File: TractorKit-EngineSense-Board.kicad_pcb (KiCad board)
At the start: 2 copper layers, 57.5 x 45 mm, 24 parts, among them J1 POWER, J2 ADC1, J3 ADC2, J4 UART, J5 I2C, U1 AMS1117-3.3, U2 ACS711xLCTR-12AB, U3 ESP32-WROOM-32

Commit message: First complete draft.
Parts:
- removed TP1: SERVICE_BOOT, TestPoint:TestPoint_Pad_D1.5mm
- removed TP2: SERVICE_TX, TestPoint:TestPoint_Pad_D1.5mm
- removed TP3: SERVICE_RX, TestPoint:TestPoint_Pad_D1.5mm
- removed TP5: SERVICE_GND, TestPoint:TestPoint_Pad_D1.5mm
- added  : , open-agri.github.io/TKES1, B.Cu at (59.8, 65.2)
- added  : MountingHole_3.2mm_M3_DIN965_Pad, MountingHole:MountingHole_3.2mm_M3_DIN965_Pad, F.Cu at (81.8, 87.0)
- added  : MountingHole_3.2mm_M3_DIN965_Pad, MountingHole:MountingHole_3.2mm_M3_DIN965_Pad, F.Cu at (124.2, 60.7)
- added  : MountingHole_3.2mm_M3_DIN965_Pad, MountingHole:MountingHole_3.2mm_M3_DIN965_Pad, F.Cu at (75.0, 61.0)
- added BOOT: SERVICE_BOOT, TestPoint:TestPoint_Pad_D1.5mm, F.Cu at (108.6, 87.6)
- added GND: SERVICE_GND, TestPoint:TestPoint_Pad_D1.5mm, F.Cu at (93.3, 87.6)
- added R10: 1k, Resistor_THT:R_Axial_DIN0207_L6.3mm_D2.5mm_P10.16mm_Horizontal, F.Cu at (122.9, 76.2)
- added R11: 1k, Resistor_THT:R_Axial_DIN0207_L6.3mm_D2.5mm_P10.16mm_Horizontal, F.Cu at (119.9, 76.2)
- added R12: 1k, Resistor_THT:R_Axial_DIN0207_L6.3mm_D2.5mm_P10.16mm_Horizontal, F.Cu at (116.8, 76.2)
- added R13: 1k, Resistor_THT:R_Axial_DIN0207_L6.3mm_D2.5mm_P10.16mm_Horizontal, F.Cu at (113.8, 76.2)
- added R4: 10k, Resistor_THT:R_Axial_DIN0207_L6.3mm_D2.5mm_P10.16mm_Horizontal, F.Cu at (126.0, 88.9)
- added R5: 10k, Resistor_THT:R_Axial_DIN0207_L6.3mm_D2.5mm_P10.16mm_Horizontal, F.Cu at (122.9, 88.9)
- added R6: 10k, Resistor_THT:R_Axial_DIN0207_L6.3mm_D2.5mm_P10.16mm_Horizontal, F.Cu at (119.9, 88.9)
- added R7: 10k, Resistor_THT:R_Axial_DIN0207_L6.3mm_D2.5mm_P10.16mm_Horizontal, F.Cu at (116.8, 88.9)
- added R8: 10k, Resistor_THT:R_Axial_DIN0207_L6.3mm_D2.5mm_P10.16mm_Horizontal, F.Cu at (113.8, 88.9)
- added R9: 1k, Resistor_THT:R_Axial_DIN0207_L6.3mm_D2.5mm_P10.16mm_Horizontal, F.Cu at (126.0, 76.2)
- added RX: SERVICE_RX, TestPoint:TestPoint_Pad_D1.5mm, F.Cu at (101.0, 87.6)
- added TX: SERVICE_TX, TestPoint:TestPoint_Pad_D1.5mm, F.Cu at (104.8, 87.6)
- moved R3 33.5 mm to (85.7, 83.8), turned to 90 degrees
- moved U1 27.5 mm to (73.7, 85.1)
- moved R1 24.8 mm to (72.4, 78.1), turned to 90 degrees
- moved 3V3 23.8 mm to (97.2, 87.6), turned to 180 degrees
- moved J3 23.3 mm to (125.0, 95.0), turned to 180 degrees
- moved C6 23.1 mm to (85.6, 66.0), turned to 180 degrees
- moved J2 22.3 mm to (110.0, 95.0), turned to 180 degrees
- moved R2 21.8 mm to (76.2, 67.9), turned to 270 degrees
- moved C1 18.6 mm to (65.4, 74.3), turned to 180 degrees
- moved C5 17.0 mm to (55.3, 64.1)
- moved C7 13.4 mm to (80.7, 69.8)
- moved C2 12.8 mm to (67.3, 87.5), turned to 90 degrees
- moved C4 11.9 mm to (54.6, 77.4), turned to 90 degrees
- moved U3 11.5 mm to (98.5, 72.9)
- moved BYPASS 5.77 mm to (62.7, 86.1)
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- renumbered TP4 to 3V3, JP1 to BYPASS
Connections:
- net Net-(J1-Pad1) renamed /12VIN
- J2 pad 1: Net-(J2-Pad1) -> /ADC1_4
- J2 pad 2: Net-(J2-Pad2) -> /ADC1_7
- J2 pad 3: Net-(J2-Pad3) -> +12V
- J3 pad 1: Net-(J3-Pad1) -> /ADC2_8
- J3 pad 2: Net-(J3-Pad2) -> /ADC2_9
- J3 pad 3: Net-(J3-Pad3) -> /ADC2_7
- J4 pad 1: Net-(J4-Pad1) -> /RX
- J4 pad 2: Net-(J4-Pad2) -> /TX
- U3 pad 27: Net-(U3-Pad27) -> /RX
- U3 pad 28: Net-(U3-Pad28) -> /TX
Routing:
- net +12V: track 0.00 -> 59.6 mm
- net /SCL: track 0.00 -> 51.3 mm
- net +3V3: track 0.00 -> 49.5 mm, vias 0 -> 2
- net /SDA: track 0.00 -> 43.3 mm
- net Net-(R4-Pad2): track 0.00 -> 41.3 mm, vias 0 -> 1
- net /AN_CURR: track 0.00 -> 40.9 mm
- net Net-(R10-Pad1): track 0.00 -> 38.4 mm, vias 0 -> 1
- net Net-(R11-Pad1): track 0.00 -> 35.5 mm, vias 0 -> 1
- net Net-(R12-Pad1): track 0.00 -> 34.1 mm, vias 0 -> 1
- net /PR_RX: track 0.00 -> 32.0 mm
- net Net-(R13-Pad1): track 0.00 -> 30.9 mm, vias 0 -> 1
- net /PR_TX: track 0.00 -> 30.3 mm
- net /TX: track 0.00 -> 27.5 mm
- net /RX: track 0.00 -> 23.3 mm
- net GND: track 0.00 -> 21.7 mm, vias 0 -> 18
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- added copper zone on F.Cu, net +12V
- added copper zone on F.Cu, net +3V3
- added copper zone on F.Cu, net /12VIN
- added copper zone on B.Cu, net GND
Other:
- board size 57.5 x 45 mm -> 76 x 45 mm
- rule pad_to_mask_clearance: 0.051 -> 0
- board text added: "+12V"
- board text added: "+3.3V"
- board text added: "0-36V, NOT PROTECTED ALL INPUTS 11k FOR ADC 2 DISABLE Wi-Fi"
- board text added: "12V POWER INPUT 3.3V OUT 1A MAX"
- board text added: "3.3V"
- board text added: "CH4"
- board text added: "CH7"
- board text added: "CH8"
- board text added: "CH9"
- board text added: "EngineSense 1.0 Riccardo Persello ©2020 OpenAgri Model number TKES1 Board S/N: JLCJLCJLCJLC"
- board text added: "GND"
- board text added: "I2C"
- board text added: "INPUT"
- board text added: "IO25"
- board text added: "IO26"
- board text added: "IO27"
- board text added: "OUT"
- board text added: "POWER"
- board text added: "RX"
- board text added: "SAR ADC 1"
- board text added: "SAR ADC 2 / GPIO"
- board text added: "SCL"
- board text added: "SDA"
- board text added: "SERIAL"
- board text added: "SERIAL/I2C 3.3V ONLY NOT PROTECTED NO 5V TOLERANCE"
- board text added: "TX"

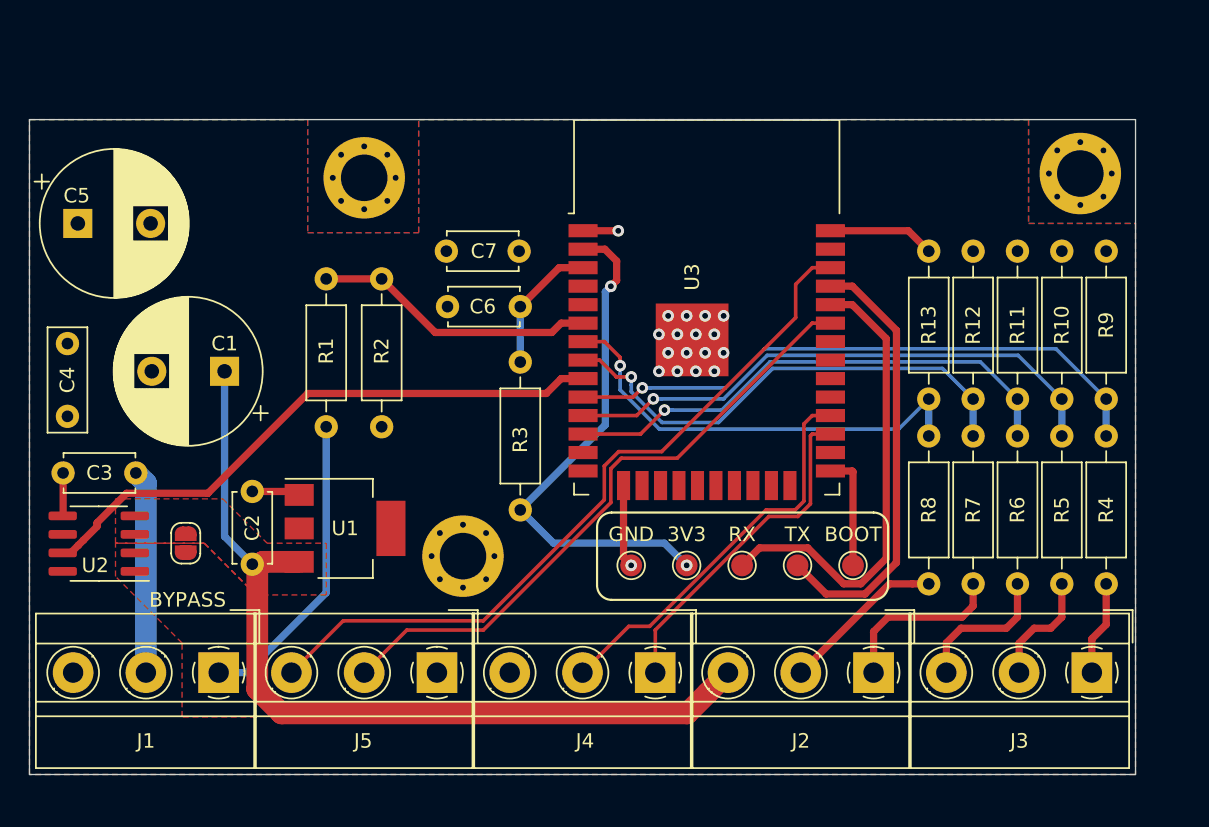
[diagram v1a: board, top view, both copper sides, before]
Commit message: Moved to SMD components
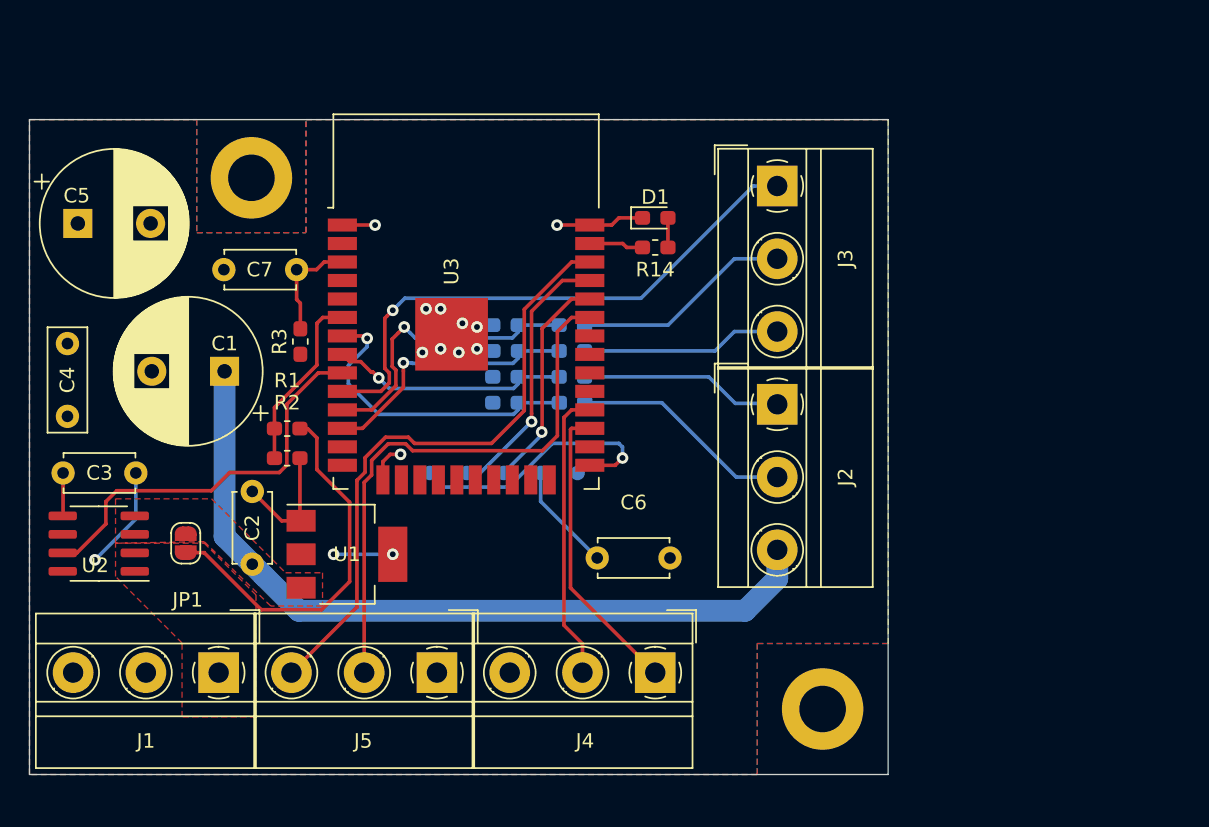
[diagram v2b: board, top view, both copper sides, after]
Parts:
- removed the   at (81.8, 87.0)
- removed the   at (124.2, 60.7)
- removed the   at (75.0, 61.0)
- removed 3V3: SERVICE_3V3, TestPoint:TestPoint_Pad_D1.5mm
- removed BOOT: SERVICE_BOOT, TestPoint:TestPoint_Pad_D1.5mm
- removed GND: SERVICE_GND, TestPoint:TestPoint_Pad_D1.5mm
- removed R4: 10k, Resistor_THT:R_Axial_DIN0207_L6.3mm_D2.5mm_P10.16mm_Horizontal
- removed R9: 1k, Resistor_THT:R_Axial_DIN0207_L6.3mm_D2.5mm_P10.16mm_Horizontal
- removed the RX at (101.0, 87.6)
- removed the TX at (104.8, 87.6)
- added  : MountingHole_3.2mm_M3_DIN965_Pad, MountingHole:MountingHole_3.2mm_M3_DIN965_Pad, F.Cu at (106.5, 97.5)
- added  : MountingHole_3.2mm_M3_DIN965_Pad, MountingHole:MountingHole_3.2mm_M3_DIN965_Pad, F.Cu at (67.2, 61.0)
- added +: SERVICE_3V3, TestPoint:TestPoint_Pad_D1.0mm, B.Cu at (87.1, 81.3)
- added -: SERVICE_GND, TestPoint:TestPoint_Pad_D1.0mm, B.Cu at (89.7, 81.3)
- added B: SERVICE_BOOT, TestPoint:TestPoint_Pad_D1.0mm, B.Cu at (79.5, 81.3)
- added D1: LED, LED_SMD:LED_0603_1608Metric_Pad1.05x0.95mm_HandSolder, F.Cu at (95.0, 63.8)
- added R14: R, Resistor_SMD:R_0603_1608Metric_Pad1.05x0.95mm_HandSolder, F.Cu at (95.0, 65.8)
- added RX: SERVICE_RX, TestPoint:TestPoint_Pad_D1.0mm, B.Cu at (84.6, 81.3)
- added TX: SERVICE_TX, TestPoint:TestPoint_Pad_D1.0mm, B.Cu at (82.0, 81.3)
-  : footprint open-agri.github.io/TKES1 -> open-agri.github.io_TKES1
- C6: value C -> 100n
- R1, R2, R3: footprint Resistor_THT:R_Axial_DIN0207_L6.3mm_D2.5mm_P10.16mm_Horizontal -> Resistor_SMD:R_0603_1608Metric_Pad1.05x0.95mm_HandSolder
- R10, R11, R12, R13, R5, R6, R7, R8: footprint Resistor_THT:R_Axial_DIN0207_L6.3mm_D2.5mm_P10.16mm_Horizontal -> Resistor_SMD:R_0603_1608Metric_Pad1.05x0.95mm_HandSolder; moved to B.Cu
- moved J3 39.8 mm to (103.4, 61.6), turned to 270 degrees
- moved R10 38.6 mm to (84.7, 71.1), turned to 180 degrees
- moved R5 38.1 mm to (89.3, 71.1), turned to 180 degrees
- moved R11 35.3 mm to (84.7, 72.9), turned to 180 degrees
- moved R6 34.6 mm to (89.3, 72.9), turned to 180 degrees
- moved R12 32.2 mm to (84.7, 74.7), turned to 180 degrees
- moved R7 31.0 mm to (89.3, 74.7), turned to 180 degrees
- moved R13 29.1 mm to (84.7, 76.5), turned to 180 degrees
- moved R8 27.5 mm to (89.3, 76.5), turned to 180 degrees
- moved C6 21.8 mm to (91.0, 87.1), turned to 0 degrees
- moved J2 19.6 mm to (103.4, 76.6), turned to 270 degrees
- moved R3 19.0 mm to (70.6, 72.2)
- moved U3 16.5 mm to (82.0, 72.5)
- moved C7 15.6 mm to (65.4, 67.3)
- moved R2 13.9 mm to (69.7, 80.3), turned to 0 degrees
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- renumbered BYPASS to JP1
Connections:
- J3 pad 1: /ADC2_8 -> /DIGITAL
- U3 pad 10: Net-(R4-Pad2) -> /DIGITAL
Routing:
- net Net-(R4-Pad2): track 41.3 -> 0.00 mm, vias 1 -> 0
- net /DIGITAL: track 0.00 -> 38.8 mm, vias 0 -> 1
- net +3V3: track 49.5 -> 18.7 mm, vias 2 -> 3
- net Net-(R10-Pad1): track 38.4 -> 20.4 mm
- net Net-(R12-Pad1): track 34.1 -> 16.5 mm
- net Net-(R11-Pad1): track 35.5 -> 18.4 mm
- net /PR_RX: track 32.0 -> 15.1 mm, vias 0 -> 1
- net /AN_CURR: track 40.9 -> 27.7 mm
- net /PR_TX: track 30.3 -> 18.4 mm, vias 0 -> 1
- net /PR_BOOT: track 8.00 -> 18.2 mm, vias 0 -> 1
- net Net-(R13-Pad1): track 30.9 -> 21.4 mm
- net /SCL: track 51.3 -> 42.3 mm
- net /TX: track 27.5 -> 20.1 mm
- net /ADC2_9: track 7.99 -> 15.1 mm
- net /AN_VOLT: track 19.4 -> 12.4 mm
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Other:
- board size 76 x 45 mm -> 59 x 45 mm
- board text added: "0-36V, NOT PROTECTED ALL INPUTS 11k, GPIO MAX 3V3 FOR ADC 2 DISABLE Wi-Fi"
- board text added: "DIG"
- board text added: "EngineSense 1.0 Riccardo Persello ©2020 OpenAgri Model number TKES1"
- board text added: "GPIO"
- board text added: "SAR ADC 2"
- board text removed: "0-36V, NOT PROTECTED ALL INPUTS 11k FOR ADC 2 DISABLE Wi-Fi"
- board text removed: "CH8"
- board text removed: "EngineSense 1.0 Riccardo Persello ©2020 OpenAgri Model number TKES1 Board S/N: JLCJLCJLCJLC"
- board text removed: "SAR ADC 2 / GPIO"

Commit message: Holes with vias
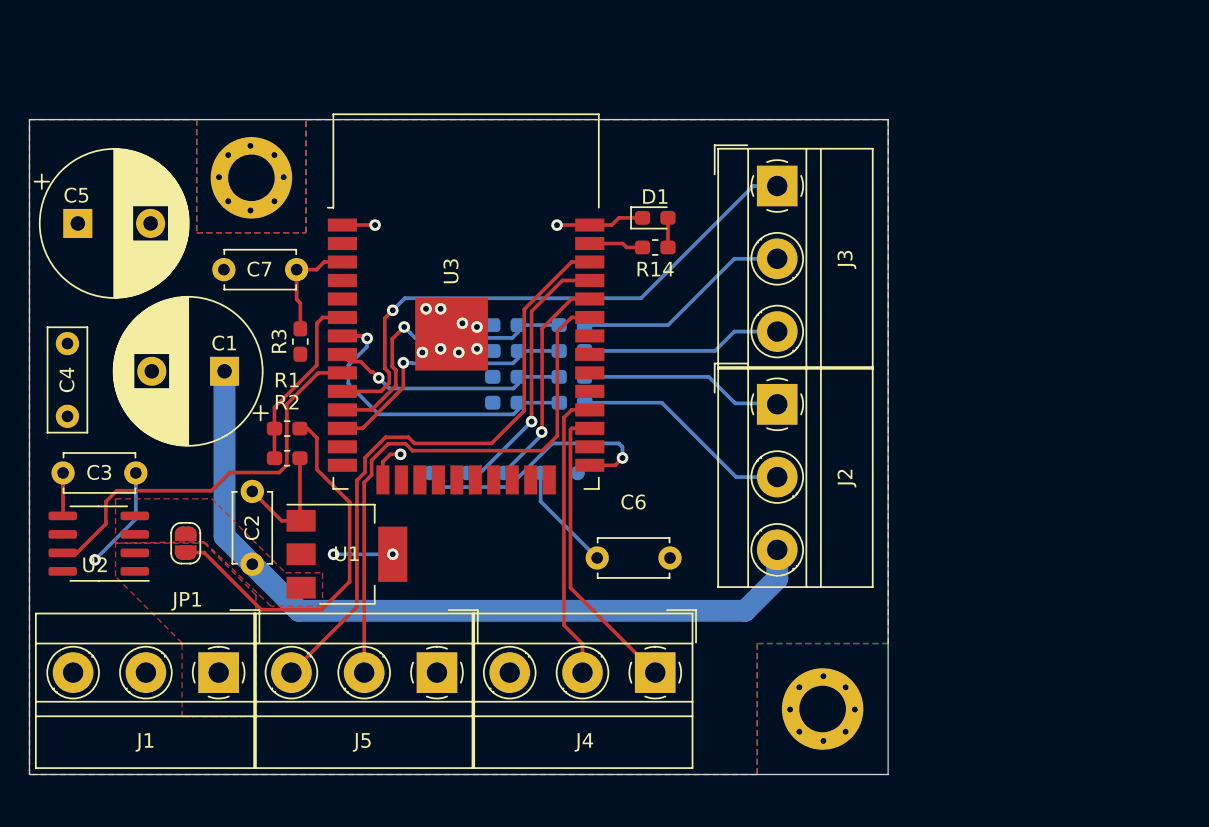
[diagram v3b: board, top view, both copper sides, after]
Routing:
- net (no net): vias 0 -> 16
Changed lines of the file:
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@@
     (thickness 1.6)
     (drawings 102)
-    (tracks 212)
+    (tracks 228)
     (zones 0)
     (modules 37)
@@
   (gr_line (start 111 102) (end 111 57) (layer Edge.Cuts) (width 0.05))
   (gr_line (start 52 102) (end 111 102) (layer Edge.Cuts) (width 0.05))
-  (via (at 76.962 86.868) (size 0.8) (drill 0.4) (layers F.Cu B.Cu) (net 3))
-  (via (at 82.75 71.25) (size 0.8) (drill 0.4) (layers F.Cu B.Cu) (net 2))
-  (via (at 82.75 72.75) (size 0.8) (drill 0.4) (layers F.Cu B.Cu) (net 2))
-  (via (at 81.5 73) (size 0.8) (drill 0.4) (layers F.Cu B.Cu) (net 2))
-  (via (at 80.25 72.75) (size 0.8) (drill 0.4) (layers F.Cu B.Cu) (net 2))
-  (via (at 79 73) (size 0.8) (drill 0.4) (layers F.Cu B.Cu) (net 2))
+  (via (at 108.712 97.536) (size 0.8) (drill 0.4) (layers F.Cu B.Cu) (net 0))
+  (via (at 104.267 97.536) (size 0.8) (drill 0.4) (layers F.Cu B.Cu) (net 0))
+  (via (at 106.553 95.25) (size 0.8) (drill 0.4) (layers F.Cu B.Cu) (net 0))
+  (via (at 106.553 99.695) (size 0.8) (drill 0.4) (layers F.Cu B.Cu) (net 0))
+  (via (at 108.077 96.012) (size 0.8) (drill 0.4) (layers F.Cu B.Cu) (net 0))
+  (via (at 104.902 96.012) (size 0.8) (drill 0.4) (layers F.Cu B.Cu) (net 0))
+  (via (at 108.077 99.06) (size 0.8) (drill 0.4) (layers F.Cu B.Cu) (net 0))
+  (via (at 104.902 99.06) (size 0.8) (drill 0.4) (layers F.Cu B.Cu) (net 0))
+  (via (at 67.183 58.801) (size 0.8) (drill 0.4) (layers F.Cu B.Cu) (net 0))
+  (via (at 67.183 63.246) (size 0.8) (drill 0.4) (layers F.Cu B.Cu) (net 0))
+  (via (at 69.469 60.96) (size 0.8) (drill 0.4) (layers F.Cu B.Cu) (net 0))
+  (via (at 65.024 60.96) (size 0.8) (drill 0.4) (layers F.Cu B.Cu) (net 0))
+  (via (at 65.659 59.436) (size 0.8) (drill 0.4) (layers F.Cu B.Cu) (net 0))
+  (via (at 68.834 59.436) (size 0.8) (drill 0.4) (layers F.Cu B.Cu) (net 0))
+  (via (at 68.834 62.611) (size 0.8) (drill 0.4) (layers F.Cu B.Cu) (net 0))
+  (via (at 65.659 62.611) (size 0.8) (drill 0.4) (layers F.Cu B.Cu) (net 0))
   (segment (start 68.109999 88.349999) (end 67.31 87.55) (width 1.5) (layer B.Cu) (net 1))
   (segment (start 101.174898 90.75) (end 70.51 90.75) (width 1.5) (layer B.Cu) (net 1))
@@
   (segment (start 65.405 85.645) (end 65.405 74.295) (width 1.5) (layer B.Cu) (net 1))
   (segment (start 67.31 87.55) (end 65.405 85.645) (width 1.5) (layer B.Cu) (net 1))
+  (via (at 82.75 71.25) (size 0.8) (drill 0.4) (layers F.Cu B.Cu) (net 2))
+  (via (at 82.75 72.75) (size 0.8) (drill 0.4) (layers F.Cu B.Cu) (net 2))
+  (via (at 81.5 73) (size 0.8) (drill 0.4) (layers F.Cu B.Cu) (net 2))
+  (via (at 80.25 72.75) (size 0.8) (drill 0.4) (layers F.Cu B.Cu) (net 2))
+  (via (at 79 73) (size 0.8) (drill 0.4) (layers F.Cu B.Cu) (net 2))
   (segment (start 54.309 84.206) (end 54.285 84.23) (width 0.25) (layer F.Cu) (net 2))
   (segment (start 54.309 81.28) (end 54.309 84.206) (width 0.25) (layer F.Cu) (net 2))
@@
   (segment (start 70.584 84.49) (end 70.662 84.568) (width 0.25) (layer F.Cu) (net 2))
   (segment (start 70.584 80.264) (end 70.584 84.49) (width 0.25) (layer F.Cu) (net 2))
+  (via (at 76.962 86.868) (size 0.8) (drill 0.4) (layers F.Cu B.Cu) (net 3))
   (segment (start 87.122 83.232) (end 91.012 87.122) (width 0.25) (layer B.Cu) (net 3))
   (segment (start 87.122 81.28) (end 87.122 83.232) (width 0.25) (layer B.Cu) (net 3))

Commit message: Ready for panelization
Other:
- board text added: "15V IN MAX 3.3V OUT 1A MAX"
- board text added: "EngineSense Riccardo Persello ©2020 OpenAgri Model number TKES"
- board text removed: "12V POWER INPUT 3.3V OUT 1A MAX"
- board text removed: "EngineSense 1.0 Riccardo Persello ©2020 OpenAgri Model number TKES1"
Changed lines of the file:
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@@
     (34 B.Paste user hide)
     (35 F.Paste user hide)
-    (36 B.SilkS user hide)
-    (37 F.SilkS user hide)
+    (36 B.SilkS user)
+    (37 F.SilkS user)
     (38 B.Mask user)
     (39 F.Mask user)
@@
   )
   (gr_line (start 101.1 64.13) (end 97.94 64.13) (layer B.SilkS) (width 0.15))
-  (gr_text "EngineSense 1.0\nRiccardo Persello\n©2020 OpenAgri\nModel number TKES1" (at 77.75 58.75 90) (layer B.SilkS)
+  (gr_text "EngineSense\nRiccardo Persello\n©2020 OpenAgri\nModel number TKES" (at 77.75 58.75 90) (layer B.SilkS)
     (effects (font (size 1 1) (thickness 0.15)) (justify left mirror))
   )
@@
     (effects (font (size 1 1) (thickness 0.15)) (justify mirror))
   )
-  (gr_text "12V POWER INPUT\n3.3V OUT 1A MAX" (at 59.944 86.106) (layer B.SilkS)
+  (gr_text "15V IN MAX\n3.3V OUT 1A MAX" (at 59.944 86.106) (layer B.SilkS)
     (effects (font (size 1 1) (thickness 0.15)) (justify mirror))
   )
